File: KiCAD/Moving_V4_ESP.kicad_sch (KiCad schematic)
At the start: 88 parts, among them J1 Vin_1, J10 Conn_01x03_Pin, J11 Conn_01x03_Pin, J12 Conn_01x03_Pin, J13 Conn_01x03_Pin, J2 Vin_2, J3 Power_SW, J4 USB_B_Micro, J5 MOTOR_R, J6 Motor_L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

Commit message: 汎用IOのフットプリントを反映
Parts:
- J10, J11, J12, J13: footprint (none) -> Connector_PinHeader_2.54mm:PinHeader_1x03_P2.54mm_Vertical
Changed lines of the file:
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@@
       (effects (font (size 1.27 1.27)))
     )
-    (property "Footprint" "" (at 167.64 246.38 0)
+    (property "Footprint" "Connector_PinHeader_2.54mm:PinHeader_1x03_P2.54mm_Vertical" (at 167.64 246.38 0)
       (effects (font (size 1.27 1.27)) hide)
     )
@@
       (effects (font (size 1.27 1.27)))
     )
-    (property "Footprint" "" (at 195.58 246.38 0)
+    (property "Footprint" "Connector_PinHeader_2.54mm:PinHeader_1x03_P2.54mm_Vertical" (at 195.58 246.38 0)
       (effects (font (size 1.27 1.27)) hide)
     )
@@
       (effects (font (size 1.27 1.27)))
     )
-    (property "Footprint" "" (at 111.76 246.38 0)
+    (property "Footprint" "Connector_PinHeader_2.54mm:PinHeader_1x03_P2.54mm_Vertical" (at 111.76 246.38 0)
       (effects (font (size 1.27 1.27)) hide)
     )
@@
       (effects (font (size 1.27 1.27)))
     )
-    (property "Footprint" "" (at 139.7 246.38 0)
-      (effects (font (size 1.27 1.27)) hide)
-    )
+    (property "Footprint" "Connector_PinHeader_2.54mm:PinHeader_1x03_P2.54mm_Vertical" (at 139.7 246.38 0)
+      (effects (font (size 1.27 1.27)) hide)
+    )

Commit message: エンコーダコネクタをZHに変更
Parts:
- J7, J8: footprint Connector_JST:JST_PH_B4B-PH-K_1x04_P2.00mm_Vertical -> YY_Common:JST_ZH_B4B-ZH-A_1x04_P1.50mm_Vertical
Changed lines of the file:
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@@
       (effects (font (size 1.27 1.27)))
     )
-    (property "Footprint" "Connector_JST:JST_PH_B4B-PH-K_1x04_P2.00mm_Vertical" (at 78.74 167.64 0)
+    (property "Footprint" "YY_Common:JST_ZH_B4B-ZH-A_1x04_P1.50mm_Vertical" (at 78.74 167.64 0)
       (effects (font (size 1.27 1.27)) hide)
     )
@@
       (effects (font (size 1.27 1.27)))
     )
-    (property "Footprint" "Connector_JST:JST_PH_B4B-PH-K_1x04_P2.00mm_Vertical" (at 78.74 185.42 0)
-      (effects (font (size 1.27 1.27)) hide)
-    )
+    (property "Footprint" "YY_Common:JST_ZH_B4B-ZH-A_1x04_P1.50mm_Vertical" (at 78.74 185.42 0)
+      (effects (font (size 1.27 1.27)) hide)
+    )

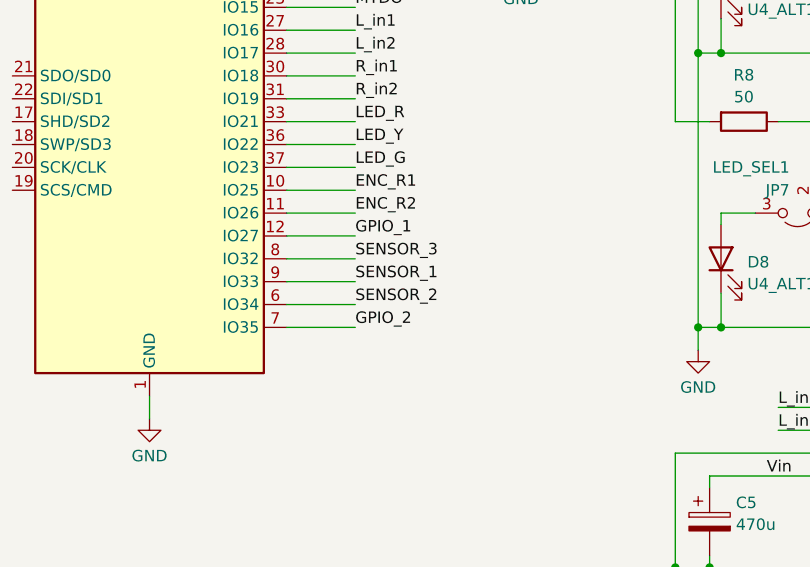
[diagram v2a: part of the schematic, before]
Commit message: 入力専用ピンがGPIOに割り振られていたため、センサ入力ピンと交換
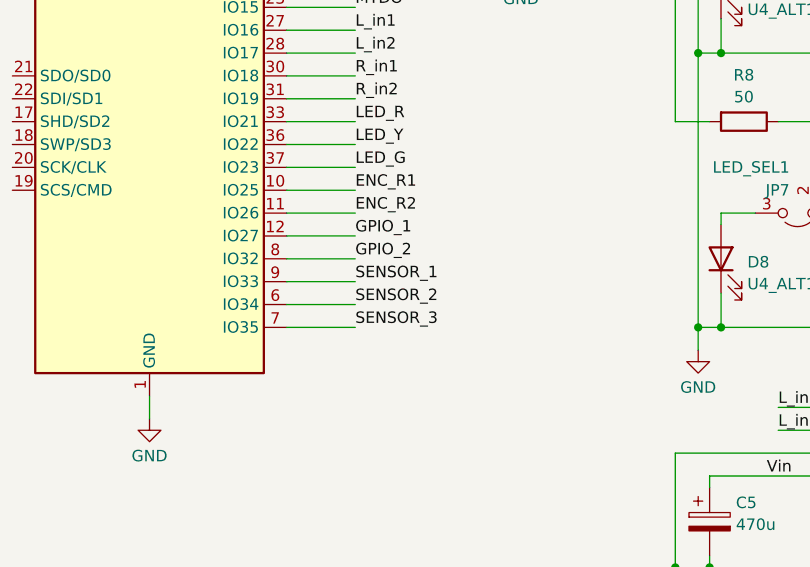
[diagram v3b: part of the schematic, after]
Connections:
- net GPIO_2: now also U3.8 (IO32); no longer U3.7 (IO35)
- net SENSOR_3: now also U3.7 (IO35); no longer U3.8 (IO32)
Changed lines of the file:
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@@
+    (effects (font (size 1.27 1.27)) (justify left bottom))
+  )
+  (label "SENSOR_3" (at 177.8 106.68 0) (fields_autoplaced)
     (effects (font (size 1.27 1.27)) (justify left bottom))
   )
@@
     (effects (font (size 1.27 1.27)) (justify left bottom))
   )
-  (label "GPIO_2" (at 177.8 106.68 0) (fields_autoplaced)
-    (effects (font (size 1.27 1.27)) (justify left bottom))
-  )
   (label "ENC_R2" (at 177.8 93.98 0) (fields_autoplaced)
     (effects (font (size 1.27 1.27)) (justify left bottom))
@@
     (effects (font (size 1.27 1.27)) (justify left bottom))
   )
-  (label "SENSOR_3" (at 177.8 99.06 0) (fields_autoplaced)
-    (effects (font (size 1.27 1.27)) (justify left bottom))
-  )
   (label "Vin" (at 175.26 223.52 0) (fields_autoplaced)
     (effects (font (size 1.27 1.27)) (justify left bottom))
@@
     (effects (font (size 1.27 1.27)) (justify left bottom))
   )
+  (label "GPIO_2" (at 177.8 99.06 0) (fields_autoplaced)
+    (effects (font (size 1.27 1.27)) (justify left bottom))
+  )

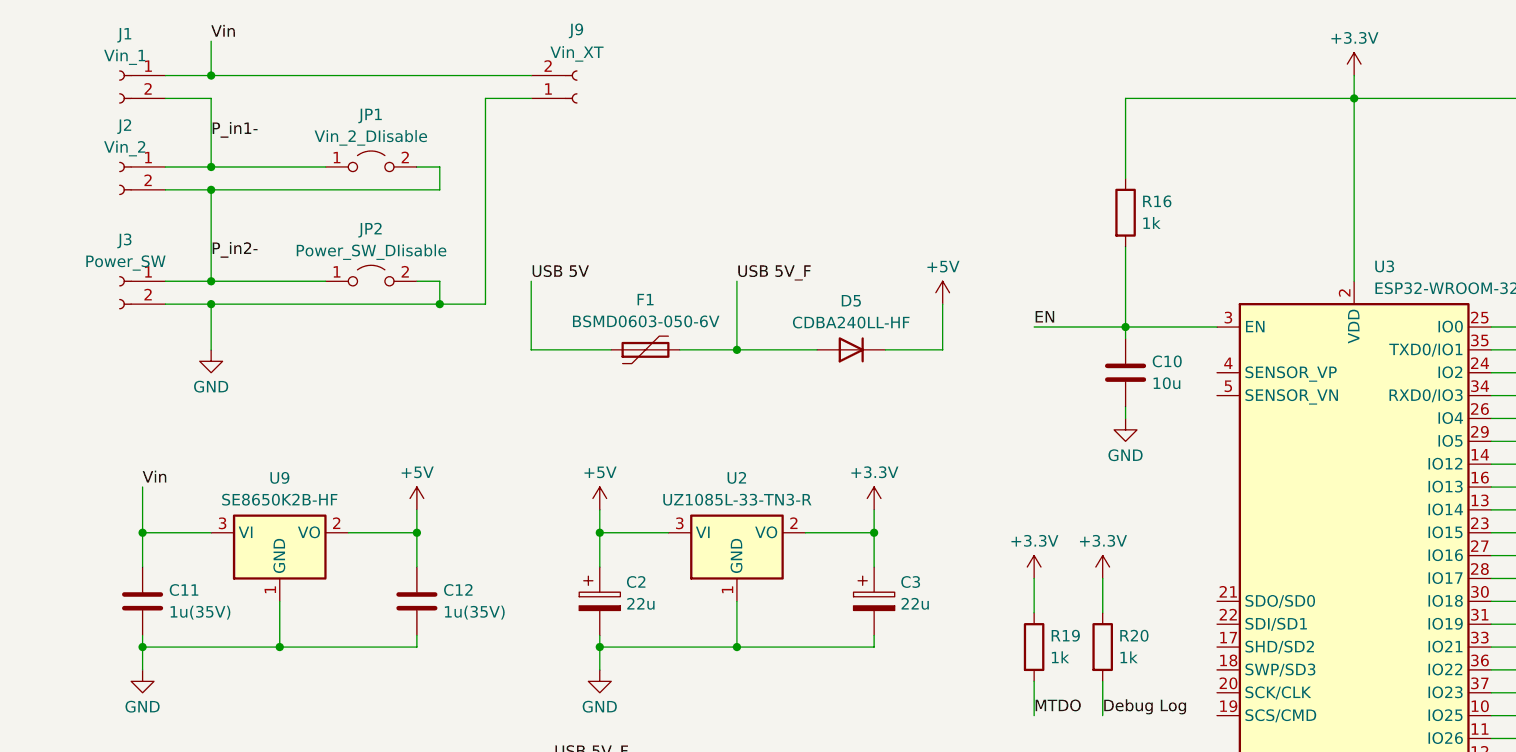
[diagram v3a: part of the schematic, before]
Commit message: 電源電圧監視回路を追加
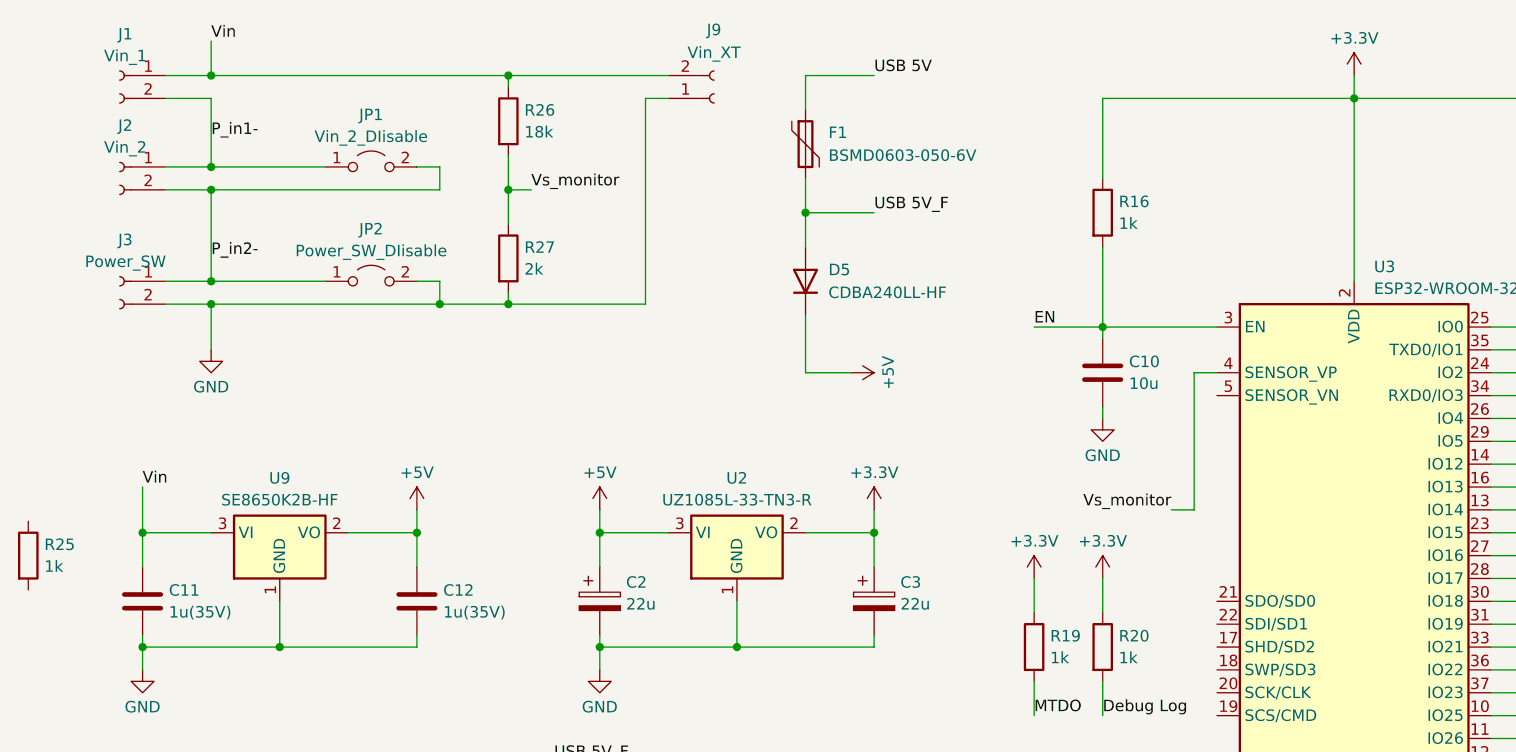
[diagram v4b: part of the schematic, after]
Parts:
- added R25: 1k, Resistor_SMD:R_0402_1005Metric, symbol Device:R
- added R26: 18k, Resistor_SMD:R_0402_1005Metric, symbol Device:R
- added R27: 2k, Resistor_SMD:R_0402_1005Metric, symbol Device:R
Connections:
- net GND: now also R27.2
- net Vin: now also R26.1
- net Vs_monitor: now reaches U3.4 (SENSOR_VP)
- net Vs_monitor: now also R26.2, R27.1
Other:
- moved on the sheet: C10, D5, F1, J9, R16

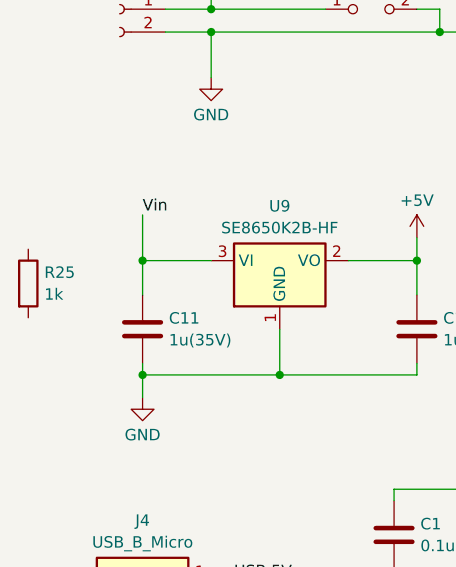
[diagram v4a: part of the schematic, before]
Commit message: 不要な抵抗を削除
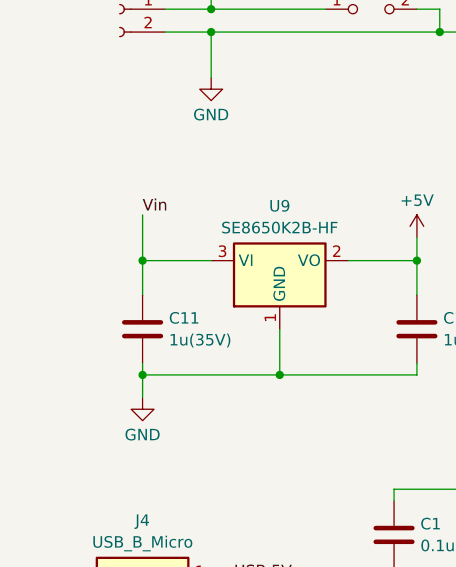
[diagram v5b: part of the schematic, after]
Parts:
- removed R25: 1k, Resistor_SMD:R_0402_1005Metric, symbol Device:R
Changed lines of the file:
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@@
-    )
-  )
-  (symbol (lib_id "Device:R") (at 7.62 73.66 0) (unit 1)
-    (in_bom yes) (on_board yes) (dnp no) (fields_autoplaced)
-    (property "Reference" "R25" (at 9.398 72.4479 0)
-      (effects (font (size 1.27 1.27)) (justify left))
-    )
-    (property "Value" "1k" (at 9.398 74.8721 0)
-      (effects (font (size 1.27 1.27)) (justify left))
-    )
-    (property "Footprint" "Resistor_SMD:R_0402_1005Metric" (at 5.842 73.66 90)
-      (effects (font (size 1.27 1.27)) hide)
-    )
-    (property "Datasheet" "~" (at 7.62 73.66 0)
-      (effects (font (size 1.27 1.27)) hide)
-    )
-    (property "LCSC" "C159872" (at 7.62 73.66 0)
-      (effects (font (size 1.27 1.27)) hide)
-    )
-    (pin "1")
-    (pin "2")
-    (instances
-      (project "Moving_V4_ESP"
-        (path "/515135d2-db88-48ff-b508-cbebeed2b019"
-          (reference "R25") (unit 1)
-        )
-      )
     )
   )

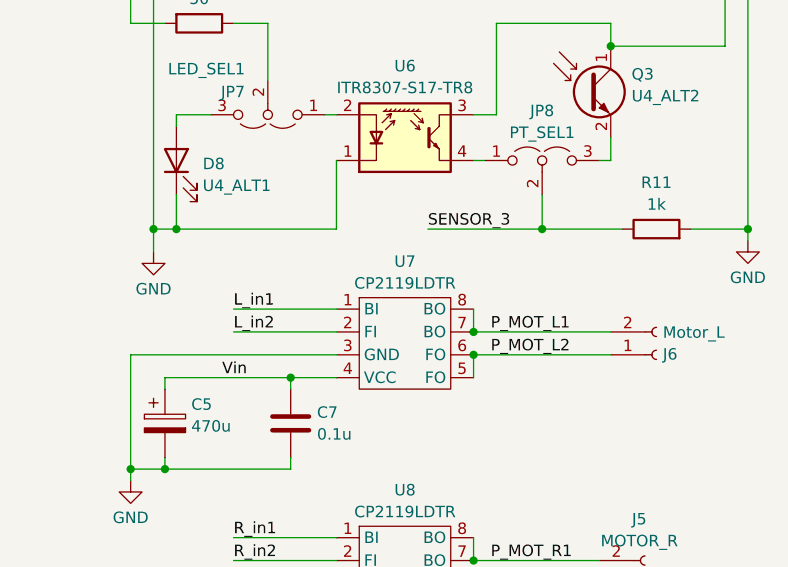
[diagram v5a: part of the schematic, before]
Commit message: モータドライバの部品名を修正
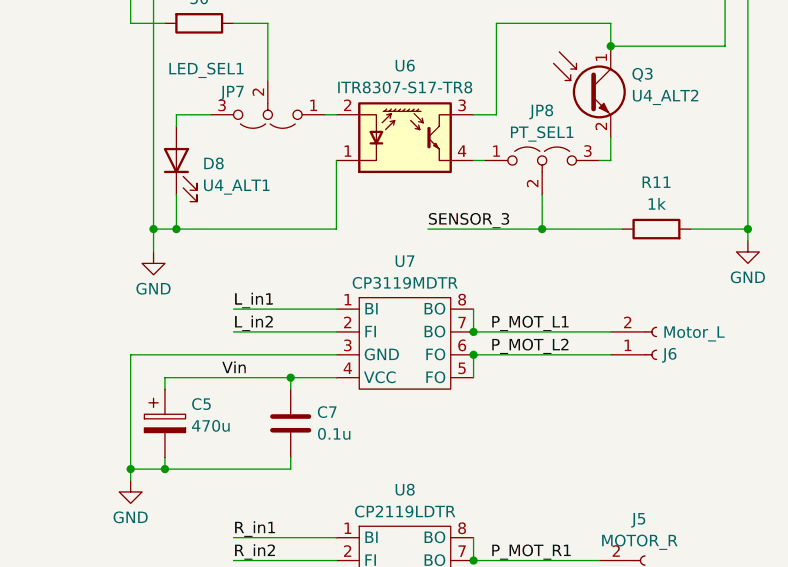
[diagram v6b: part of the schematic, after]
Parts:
- U7: value CP2119LDTR -> CP3119MDTR; LCSC C42395498 -> C42395499
- U8: LCSC C42395498 -> C42395499
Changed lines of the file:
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@@
       (effects (font (size 1.27 1.27)))
     )
-    (property "Value" "CP2119LDTR" (at 243.84 112.7069 0)
+    (property "Value" "CP3119MDTR" (at 243.84 112.7069 0)
       (effects (font (size 1.27 1.27)))
     )
@@
       (effects (font (size 1.27 1.27)) hide)
     )
-    (property "LCSC" "C42395498" (at 243.84 119.38 0)
+    (property "LCSC" "C42395499" (at 243.84 119.38 0)
       (effects (font (size 1.27 1.27)) hide)
     )
@@
       (effects (font (size 1.27 1.27)) hide)
     )
-    (property "LCSC" "C42395498" (at 243.84 144.78 0)
-      (effects (font (size 1.27 1.27)) hide)
-    )
+    (property "LCSC" "C42395499" (at 243.84 144.78 0)
+      (effects (font (size 1.27 1.27)) hide)
+    )
